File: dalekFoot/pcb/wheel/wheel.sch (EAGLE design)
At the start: 49 parts, among them IC1 LM1117MP-3.3, IC2 LM1117MP-3.3, IC3 LM1117MP-3.3, IC4 4051D, IC5 4051D, U1 TB6612FNG(O,C,8,EL

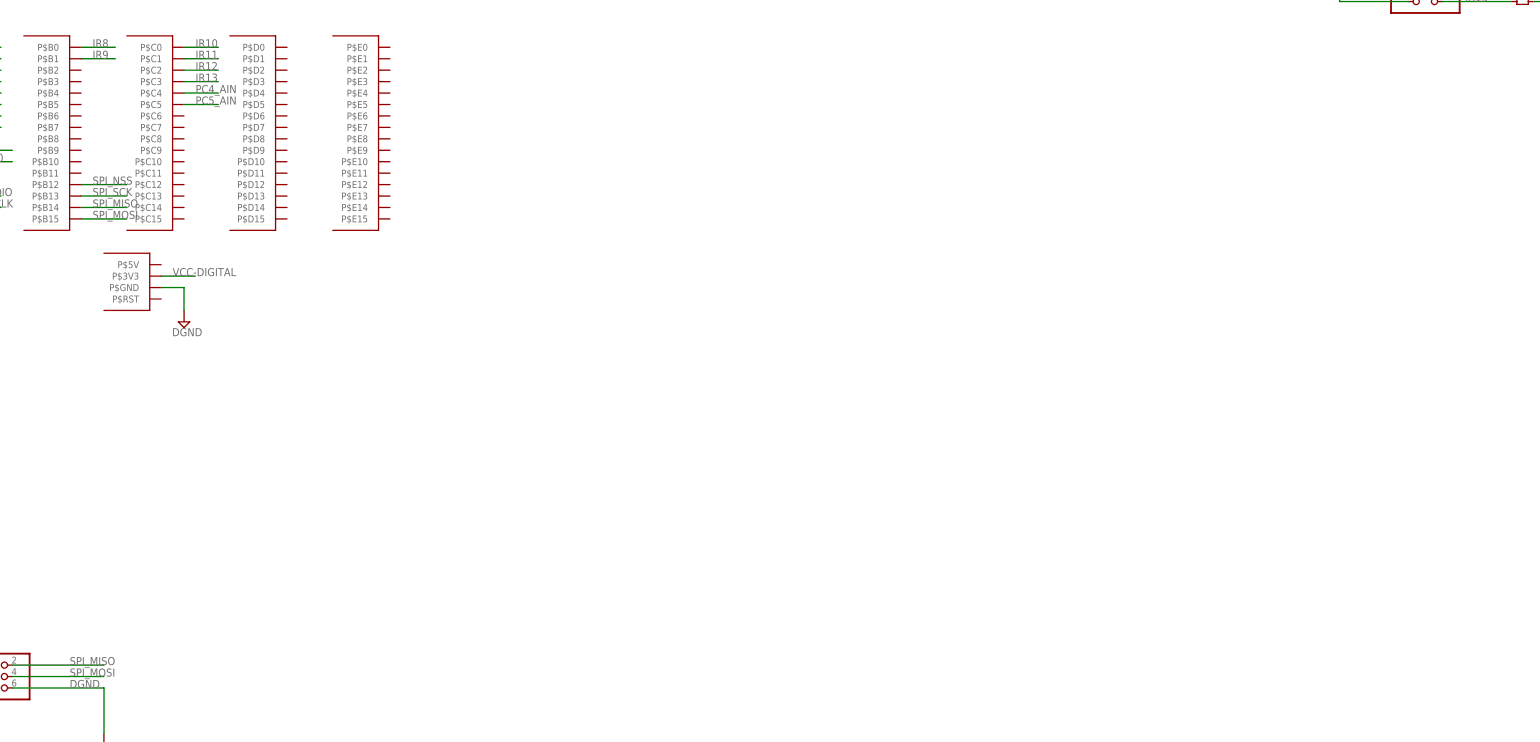
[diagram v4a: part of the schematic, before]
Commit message: add encoder port
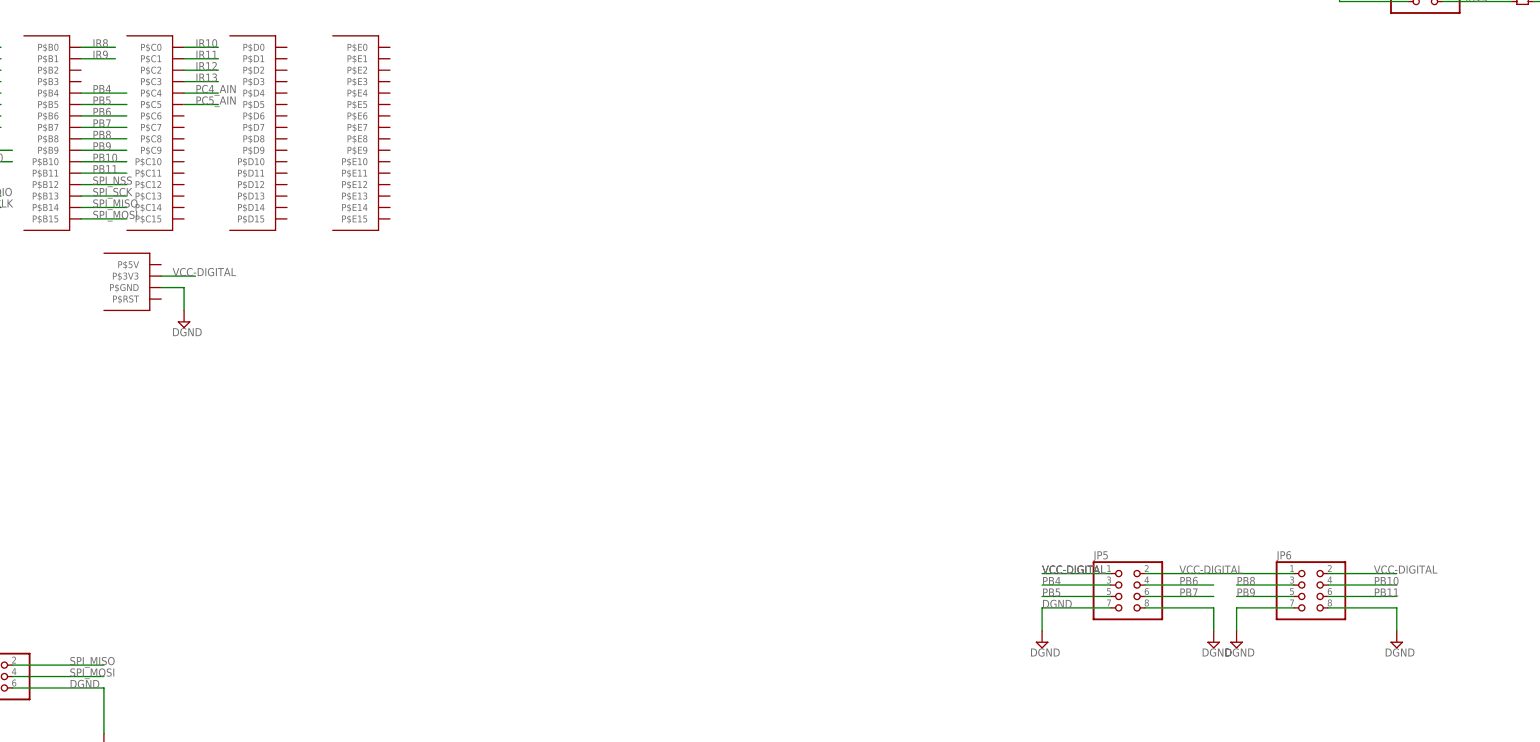
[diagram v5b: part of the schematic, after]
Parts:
- added JP5, JP6: (no value), pinhead:PINHD-2X4
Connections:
- new net PB10: JP6.4, U$1.P$B10
- new net PB11: JP6.6, U$1.P$B11
- new net PB4: JP5.3, U$1.P$B4
- new net PB5: JP5.5, U$1.P$B5
- new net PB6: JP5.4, U$1.P$B6
- new net PB7: JP5.6, U$1.P$B7
- new net PB8: JP6.3, U$1.P$B8
- new net PB9: JP6.5, U$1.P$B9
- net DGND: now also JP5.7, JP5.8, JP6.7, JP6.8
- net VCC-DIGITAL: now also JP5.1, JP5.2, JP6.1, JP6.2
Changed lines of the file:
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@@
 <part name="R28" library="rcl" deviceset="R-EU_" device="R0402"/>
 <part name="SUPPLY20" library="supply2" deviceset="DGND" device=""/>
+<part name="JP5" library="pinhead" deviceset="PINHD-2X4" device=""/>
+<part name="JP6" library="pinhead" deviceset="PINHD-2X4" device=""/>
+<part name="SUPPLY21" library="supply2" deviceset="DGND" device=""/>
+<part name="SUPPLY22" library="supply2" deviceset="DGND" device=""/>
+<part name="SUPPLY23" library="supply2" deviceset="DGND" device=""/>
+<part name="SUPPLY24" library="supply2" deviceset="DGND" device=""/>
 </parts>
 <sheets>
@@
 <instance part="R28" gate="G$1" x="12.7" y="-431.8"/>
 <instance part="SUPPLY20" gate="G$1" x="17.78" y="-454.66"/>
+<instance part="JP5" gate="A" x="320.04" y="-375.92"/>
+<instance part="JP6" gate="A" x="360.68" y="-375.92"/>
+<instance part="SUPPLY21" gate="G$1" x="302.26" y="-386.08"/>
+<instance part="SUPPLY22" gate="G$1" x="340.36" y="-386.08"/>
+<instance part="SUPPLY23" gate="G$1" x="345.44" y="-386.08"/>
+<instance part="SUPPLY24" gate="G$1" x="381" y="-386.08"/>
 </instances>
 <busses>
@@
 <pinref part="SUPPLY20" gate="G$1" pin="DGND"/>
 </segment>
+<segment>
+<pinref part="JP5" gate="A" pin="7"/>
+<wire x1="317.5" y1="-378.46" x2="302.26" y2="-378.46" width="0.1524" layer="91"/>
+<label x="302.26" y="-378.46" size="1.778" layer="95"/>
+<pinref part="SUPPLY21" gate="G$1" pin="DGND"/>
+<wire x1="302.26" y1="-378.46" x2="302.26" y2="-383.54" width="0.1524" layer="91"/>
+</segment>
+<segment>
+<pinref part="JP5" gate="A" pin="8"/>
+<wire x1="325.12" y1="-378.46" x2="340.36" y2="-378.46" width="0.1524" layer="91"/>
+<pinref part="SUPPLY22" gate="G$1" pin="DGND"/>
+<wire x1="340.36" y1="-378.46" x2="340.36" y2="-383.54" width="0.1524" layer="91"/>
+</segment>
+<segment>
+<pinref part="JP6" gate="A" pin="7"/>
+<wire x1="345.44" y1="-378.46" x2="358.14" y2="-378.46" width="0.1524" layer="91"/>
+<pinref part="SUPPLY23" gate="G$1" pin="DGND"/>
+<wire x1="345.44" y1="-378.46" x2="345.44" y2="-383.54" width="0.1524" layer="91"/>
+</segment>
+<segment>
+<pinref part="JP6" gate="A" pin="8"/>
+<wire x1="365.76" y1="-378.46" x2="381" y2="-378.46" width="0.1524" layer="91"/>
+<pinref part="SUPPLY24" gate="G$1" pin="DGND"/>
+<wire x1="381" y1="-378.46" x2="381" y2="-383.54" width="0.1524" layer="91"/>
+</segment>
 </net>
 <net name="BAT+" class="0">
@@
 <wire x1="7.62" y1="-431.8" x2="-7.62" y2="-431.8" width="0.1524" layer="91"/>
 <label x="-7.62" y="-431.8" size="1.778" layer="95"/>
+</segment>
+<segment>
+<pinref part="JP5" gate="A" pin="1"/>
+<wire x1="317.5" y1="-370.84" x2="302.26" y2="-370.84" width="0.1524" layer="91"/>
+<label x="302.26" y="-370.84" size="1.778" layer="95"/>
+<label x="302.26" y="-370.84" size="1.778" layer="95"/>
+</segment>
+<segment>
+<pinref part="JP5" gate="A" pin="2"/>
+<label x="332.74" y="-370.84" size="1.778" layer="95"/>
+<pinref part="JP6" gate="A" pin="1"/>
+<wire x1="358.14" y1="-370.84" x2="325.12" y2="-370.84" width="0.1524" layer="91"/>
+</segment>
+<segment>
+<pinref part="JP6" gate="A" pin="2"/>
+<wire x1="365.76" y1="-370.84" x2="381" y2="-370.84" width="0.1524" layer="91"/>
+<label x="375.92" y="-370.84" size="1.778" layer="95"/>
 </segment>
 </net>
@@
 </segment>
 </net>
+<net name="PB8" class="0">
+<segment>
+<pinref part="U$1" gate="G$1" pin="P$B8"/>
+<wire x1="88.9" y1="-274.32" x2="99.06" y2="-274.32" width="0.1524" layer="91"/>
+<label x="91.44" y="-274.32" size="1.778" layer="95"/>
+</segment>
+<segment>
+<pinref part="JP6" gate="A" pin="3"/>
+<wire x1="345.44" y1="-373.38" x2="358.14" y2="-373.38" width="0.1524" layer="91"/>
+<label x="345.44" y="-373.38" size="1.778" layer="95"/>
+</segment>
+</net>
+<net name="PB9" class="0">
+<segment>
+<pinref part="U$1" gate="G$1" pin="P$B9"/>
+<wire x1="88.9" y1="-276.86" x2="99.06" y2="-276.86" width="0.1524" layer="91"/>
+<label x="91.44" y="-276.86" size="1.778" layer="95"/>
+</segment>
+<segment>
+<pinref part="JP6" gate="A" pin="5"/>
+<wire x1="358.14" y1="-375.92" x2="345.44" y2="-375.92" width="0.1524" layer="91"/>
+<label x="345.44" y="-375.92" size="1.778" layer="95"/>
+</segment>
+</net>
+<net name="PB10" class="0">
+<segment>
+<pinref part="U$1" gate="G$1" pin="P$B10"/>
+<wire x1="88.9" y1="-279.4" x2="99.06" y2="-279.4" width="0.1524" layer="91"/>
+<label x="91.44" y="-279.4" size="1.778" layer="95"/>
+</segment>
+<segment>
+<pinref part="JP6" gate="A" pin="4"/>
+<wire x1="365.76" y1="-373.38" x2="381" y2="-373.38" width="0.1524" layer="91"/>
+<label x="375.92" y="-373.38" size="1.778" layer="95"/>
+</segment>
+</net>
+<net name="PB11" class="0">
+<segment>
+<pinref part="U$1" gate="G$1" pin="P$B11"/>
+<wire x1="88.9" y1="-281.94" x2="99.06" y2="-281.94" width="0.1524" layer="91"/>
+<label x="91.44" y="-281.94" size="1.778" layer="95"/>
+</segment>
+<segment>
+<pinref part="JP6" gate="A" pin="6"/>
+<wire x1="365.76" y1="-375.92" x2="381" y2="-375.92" width="0.1524" layer="91"/>
+<label x="375.92" y="-375.92" size="1.778" layer="95"/>
+</segment>
+</net>
+<net name="PB4" class="0">
+<segment>
+<pinref part="U$1" gate="G$1" pin="P$B4"/>
+<wire x1="88.9" y1="-264.16" x2="99.06" y2="-264.16" width="0.1524" layer="91"/>
+<label x="91.44" y="-264.16" size="1.778" layer="95"/>
+</segment>
+<segment>
+<pinref part="JP5" gate="A" pin="3"/>
+<wire x1="317.5" y1="-373.38" x2="302.26" y2="-373.38" width="0.1524" layer="91"/>
+<label x="302.26" y="-373.38" size="1.778" layer="95"/>
+</segment>
+</net>
+<net name="PB5" class="0">
+<segment>
+<pinref part="U$1" gate="G$1" pin="P$B5"/>
+<wire x1="88.9" y1="-266.7" x2="99.06" y2="-266.7" width="0.1524" layer="91"/>
+<label x="91.44" y="-266.7" size="1.778" layer="95"/>
+</segment>
+<segment>
+<pinref part="JP5" gate="A" pin="5"/>
+<wire x1="302.26" y1="-375.92" x2="317.5" y2="-375.92" width="0.1524" layer="91"/>
+<label x="302.26" y="-375.92" size="1.778" layer="95"/>
+</segment>
+</net>
+<net name="PB6" class="0">
+<segment>
+<pinref part="U$1" gate="G$1" pin="P$B6"/>
+<wire x1="88.9" y1="-269.24" x2="99.06" y2="-269.24" width="0.1524" layer="91"/>
+<label x="91.44" y="-269.24" size="1.778" layer="95"/>
+</segment>
+<segment>
+<pinref part="JP5" gate="A" pin="4"/>
+<wire x1="325.12" y1="-373.38" x2="340.36" y2="-373.38" width="0.1524" layer="91"/>
+<label x="332.74" y="-373.38" size="1.778" layer="95"/>
+</segment>
+</net>
+<net name="PB7" class="0">
+<segment>
+<pinref part="U$1" gate="G$1" pin="P$B7"/>
+<wire x1="88.9" y1="-271.78" x2="99.06" y2="-271.78" width="0.1524" layer="91"/>
+<label x="91.44" y="-271.78" size="1.778" layer="95"/>
+</segment>
+<segment>
+<pinref part="JP5" gate="A" pin="6"/>
+<wire x1="325.12" y1="-375.92" x2="340.36" y2="-375.92" width="0.1524" layer="91"/>
+<label x="332.74" y="-375.92" size="1.778" layer="95"/>
+</segment>
+</net>

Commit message: all components finished
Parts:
- added B1: BUZZER-12-6.6, hqc:BUZZER-12-6.6
- added C7: (no value), hqc:C-0805
- added J2: (no value), hqc:KF250-2X12P
- added K1, K2, K3, K4, K5: 12X12-TACTILE, hqc:12X12-TACTILE
- added LED1, LED2: (no value), led:LEDCHIP-LED0805
- added R29, R30, R31, R32, R33, R34: (no value), hqc:R-0805
- added U2, U3, U4: SS8050-SOT-23, hqc:SS8050-SOT-23
- added U5, U6: TB6612FNG(O,C,8,EL, TB6612FNG:TB6612FNG(O,C,8,EL
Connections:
- removed net N$2: U1.AO1@1, U1.AO1@2
- removed net N$3: U1.AO2@1, U1.AO2@2
- removed net N$6: U1.BO1@1, U1.BO1@2
- removed net N$8: U1.BO2@1, U1.BO2@2
- new net AIN1.1: U$1.P$D0, U1.AIN1
- new net AIN1.2: U$1.P$D1, U1.AIN2
- new net AIN2.1: U$1.P$D4, U5.AIN1
- new net AIN2.2: U$1.P$D5, U5.AIN2
- new net AIN3.1: U$1.P$D8, U6.AIN1
- new net AIN3.2: U$1.P$D9, U6.AIN2
- new net AO1.1: J2.P$1, U1.AO1@1, U1.AO1@2
- new net AO1.2: J2.P$3, U1.AO2@1, U1.AO2@2
- new net AO2.1: J2.P$9, U5.AO1@1, U5.AO1@2
- new net AO2.2: J2.P$11, U5.AO2@1, U5.AO2@2
- new net AO3.1: J2.P$17, U6.AO1@1, U6.AO1@2
- new net AO3.2: J2.P$19, U6.AO2@1, U6.AO2@2
- new net BIN1.1: U$1.P$D2, U1.BIN1
- new net BIN1.2: U$1.P$D3, U1.BIN2
- new net BIN2.1: U$1.P$D6, U5.BIN1
- new net BIN2.2: U$1.P$D7, U5.BIN2
- new net BIN3.1: U$1.P$D10, U6.BIN1
- new net BIN3.2: U$1.P$D11, U6.BIN2
- new net BO1.1: J2.P$5, U1.BO1@1, U1.BO1@2
- new net BO1.2: J2.P$7, U1.BO2@1, U1.BO2@2
- new net BO2.1: J2.P$13, U5.BO1@1, U5.BO1@2
- new net BO2.2: J2.P$15, U5.BO2@1, U5.BO2@2
- new net BO3.1: J2.P$21, U6.BO1@1, U6.BO1@2
- new net BO3.2: J2.P$23, U6.BO2@1, U6.BO2@2
- new net BUT1: K1.P$1, U$1.P$E0
- new net BUT2: K2.P$1, U$1.P$E1
- new net BUT3: K3.P$1, U$1.P$E2
- new net BUT4: K4.P$1, U$1.P$E3
- new net BUT5: K5.P$1, U$1.P$E4
- new net LED1: R30.P$1, U$1.P$C6
- new net LED2: R31.P$1, U$1.P$C7
- new net N$10: R30.P$2, U3.P$B
- new net N$11: R31.P$2, U4.P$B
- new net N$12: C7.P$2, U2.P$B
- new net N$15: R32.P$1, U2.P$C
- new net N$16: R33.P$1, U3.P$C
- new net N$17: R34.P$1, U4.P$C
- new net N$18: B1.P$-, R32.P$2
- new net N$20: LED1.C, R33.P$2
- new net N$21: LED2.C, R34.P$2
- new net N$25: U$1.P$C10
- new net N$26: U$1.P$C11
- new net N$27: U$1.P$C12
- new net N$28: U$1.P$C13
- new net N$29: U$1.P$C14
- new net N$30: U$1.P$C15
- new net N$58: IC4A.C
- new net N$9: C7.P$1, R29.P$2
- new net PA8: R29.P$1, U$1.P$A8
- new net PWM1.A: U$1.P$D12, U1.PWMA
- new net PWM1.B: U$1.P$D13
- new net PWM2.A: U$1.P$D14, U5.PWMA
- new net PWM2.B: U$1.P$D15, U1.PWMB, U5.PWMB
- new net PWM3.A: U$1.P$C8, U6.PWMA
- new net PWM3.B: U$1.P$C9, U6.PWMB
- net BAT+: now also U5.VM1, U5.VM2, U5.VM3, U6.VM1, U6.VM2, U6.VM3
- net DGND: now also J2.P$10, J2.P$12, J2.P$14, J2.P$16, J2.P$18, J2.P$2, J2.P$20, J2.P$22, J2.P$24, J2.P$4, J2.P$6, J2.P$8, K1.P$2, K2.P$2, K3.P$2, K4.P$2, K5.P$2, U2.P$E, U3.P$E, U4.P$E, U5.GND, U5.PGND1@1, U5.PGND1@2, U5.PGND2@1, U5.PGND2@2, U6.GND, U6.PGND1@1, U6.PGND1@2, U6.PGND2@1, U6.PGND2@2
- net VCC-DIGITAL: now also B1.P$+, LED1.A, LED2.A, U5.STBY, U5.VCC, U6.STBY, U6.VCC
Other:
- note added: "Analog"
- note added: "Communication"
- note added: "Encoder"
- note added: "Mcu"
- note added: "Motor"
- note added: "TODO: 1. add buttons"
- note added: "User Interface"
- moved on the sheet: C1, C2, C3, C4, C5, C6, D1, D2, D3, IC1, IC2, IC3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
